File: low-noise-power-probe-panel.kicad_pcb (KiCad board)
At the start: 4 copper layers, 79.8 x 124.8 mm, 118 parts, among them J1 Amphenol 031-5431-10RFX, J10 RF Shield Clip, J11 RF Shield Clip, J12 RF Shield Clip, J2 Amphenol 031-5431-10RFX, J3 Barrel_Jack, J4 USB_C_Receptacle, J5 CONN_041X04_NO_SILK, J6 RF Shield Clip, J7 RF Shield Clip, J8 RF Shield Clip, J9 RF Shield Clip, Q1 WSE3099, SW1 SW_3PDT_x3, U1 OPA322, U2 OPA322, U3 ADP7142AUJZ-2.5, U4 MCP73213T-A6SI/MF, U5 ADP7182AUJZ-2.5, U6 HUSB238, U7 LM334DT, U8 LM311DR

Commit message: add panel and gerbers for v2.0
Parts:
- removed C19: 27pF, Capacitor_SMD:C_0201_0603Metric
- removed C26: DNP, Capacitor_SMD:C_0402_1005Metric
- removed C27, C28: 4.7u, Capacitor_SMD:C_0805_2012Metric
- removed J10, J6, J7: RF Shield Clip, misc:ICSRC6508-015SFR
- removed J5: CONN_041X04_NO_SILK, Connector_PinHeader_2.54mm:PinHeader_1x04_P2.54mm_Vertical
- removed R25: 6.04k, Resistor_SMD:R_0603_1608Metric
- removed TP14: U1_OUT, rf-connectors:U.FL-Hirose
- removed TP16: V_UNREG, rf-connectors:U.FL-Hirose
- removed TP17: +V_BATCHG, rf-connectors:U.FL-Hirose
- removed TP18: +V_BAT, rf-connectors:U.FL-Hirose
- removed TP19: -V_BAT, rf-connectors:U.FL-Hirose
- added C15: 100n, Capacitor_SMD:C_0402_1005Metric, B.Cu at (230.5, 76.1)
- added C16: 100n, Capacitor_SMD:C_0402_1005Metric, B.Cu at (240.3, 75.2)
- added C17: 100n, Capacitor_SMD:C_0402_1005Metric, B.Cu at (237.7, 77.5)
- added C23: 100n, Capacitor_SMD:C_0402_1005Metric, B.Cu at (205.7, 100.4)
- added F3: SMD1206-050C-24V, Fuse:Fuse_1206_3216Metric, B.Cu at (189.2, 106.0)
- added F4: SMD1206-050C-24V, Fuse:Fuse_1206_3216Metric, B.Cu at (208.2, 106.0)
- added JP1: SolderJumper_2_Bridged, Jumper:SolderJumper-2_P1.3mm_Bridged_RoundedPad1.0x1.5mm, B.Cu at (233.5, 81.7)
- added Q2: HL2312, Package_TO_SOT_SMD:SOT-23, B.Cu at (210.4, 99.9)
- added Q3: HL2312, Package_TO_SOT_SMD:SOT-23, B.Cu at (210.4, 96.4)
- added R11: 100R, Resistor_SMD:R_0603_1608Metric, B.Cu at (230.2, 77.4)
- added R27: 160R, Resistor_SMD:R_0603_1608Metric, B.Cu at (239.8, 76.5)
- added R28: 260R, Resistor_SMD:R_0603_1608Metric, B.Cu at (239.8, 78.1)
- added R29: 100R, Resistor_SMD:R_0603_1608Metric, B.Cu at (239.8, 79.7)
- added R30: 50k, Resistor_SMD:R_0603_1608Metric, B.Cu at (230.2, 79.0)
- added R31: 1k, Resistor_SMD:R_0603_1608Metric, B.Cu at (204.7, 97.5)
- added R32: 100R, Resistor_SMD:R_0603_1608Metric, B.Cu at (207.0, 100.9)
- added R33: 100R, Resistor_SMD:R_0603_1608Metric, B.Cu at (204.4, 100.9)
- added REF**: MountingHole_3.2mm_M3, MountingHole:MountingHole_3.2mm_M3, F.Cu at (177.8, 73.5)
- added REF**: MountingHole_3.2mm_M3, MountingHole:MountingHole_3.2mm_M3, F.Cu at (219.8, 73.5)
- added U10: S-82C2AAB-I6T1U7, misc:S-82C2A_Battery_Protection_2S, B.Cu at (206.8, 97.5)
- added U9: ~, Package_SON:VSON-8-1EP_3x3mm_P0.65mm_EP1.65x2.4mm, B.Cu at (235.1, 78.2)
- C1, C22, C25, C3, J11, J12, J8, J9, R1, R2, R26, R3, R4, R5, R6, R7, U1, U2: moved to F.Cu
- C18, C20: value DNP -> 100n
- C29, C30: moved to B.Cu
- F1, F2: value 30V 500mA 150ms -> SMD1206-050C-24V
- J1, J2: value Amphenol 031-5431-10RFX -> Amphenol 132203-12; footprint rf-connectors:BNC_Amphenol_031-5431-10RFX_Horizontal -> Connector_Coaxial:SMA_Amphenol_132203-12_Horizontal
- J3: value Barrel_Jack -> DC-005 2.0
- L1: footprint Inductor_SMD:L_1210_3225Metric -> Inductor_SMD:L_1812_4532Metric; moved to F.Cu
- R15: value 6.04k -> 10M; moved to F.Cu
- R23: value 50k -> 1k
- TP1, TP12, TP2: footprint TestPoint:TestPoint_Keystone_5000-5004_Miniature -> TestPoint:TestPoint_Pad_D2.0mm; moved to F.Cu
- TP3, TP4, TP7, TP8, TP9: footprint TestPoint:TestPoint_Keystone_5000-5004_Miniature -> TestPoint:TestPoint_Pad_D2.0mm
- moved R15 60.6 mm to (199.6, 120.8), turned to 180 degrees
- moved C2 55.2 mm to (236.1, 80.5), turned to 0 degrees
- moved C18 53.1 mm to (232.3, 77.5), turned to -90 degrees
- moved TP8 20.6 mm to (218.2, 114.4)
- moved TP3 18.6 mm to (198.6, 114.4)
- moved C29 17.5 mm to (201.2, 125.2)
- moved TP5 17.5 mm to (204.7, 123.1), turned to 90 degrees
- moved C20 17.2 mm to (203.1, 100.4), turned to 90 degrees
- moved TP10 16.0 mm to (212.1, 123.1), turned to 90 degrees
- moved TP4 15.6 mm to (199.8, 121.4)
- moved TP9 14.2 mm to (217.0, 121.4)
- moved C4 14.0 mm to (207.2, 124.3), turned to -90 degrees
- moved R26 13.2 mm to (200.9, 119.2), turned to 0 degrees
- moved J8 13.0 mm to (190.4, 123.7), turned to 90 degrees
- moved C8 12.5 mm to (205.2, 119.2)
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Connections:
- net Board_0-Net-(BT1A--) renamed Board_0-/MID_BAT_D
- net Board_0-Net-(C26-Pad2) renamed Board_0-Net-(L1-Pad1)
- C18 pad 1: Board_0-Net-(J1-In) -> Board_0-/USB_VGND
- C18 pad 2: Board_0-Net-(C1-Pad2) -> Board_0-/BAL_VDD
- C2 pad 1: Board_0-/PROBE_VGND -> Board_0-/USB_VGND
- C2 pad 2: Board_0-Net-(C2-Pad2) -> Board_0-Net-(U9-CD)
- C20 pad 1: Board_0-Net-(U1--) -> Board_0-/-V_BAT_D
- C20 pad 2: Board_0-Net-(TP14-SIGNAL) -> Board_0-Net-(U10-VC)
- R15 pad 1: Board_0-/SDA -> Board_0-Net-(U1--)
- R15 pad 2: Board_0-Net-(J5-Pin_1) -> Board_0-/PROBE_VGND
- R26 pad 2: Board_0-Net-(TP14-SIGNAL) -> Board_0-Net-(R26-Pad2)
- R3 pad 1: Board_0-Net-(TP14-SIGNAL) -> Board_0-Net-(R26-Pad2)
- R5 pad 2: Board_0-Net-(C2-Pad2) -> Board_0-Net-(R5-Pad2)
- R6 pad 2: Board_0-Net-(TP14-SIGNAL) -> Board_0-Net-(R26-Pad2)
- RV1 pad 2: Board_0-Net-(C2-Pad2) -> Board_0-Net-(R5-Pad2)
- SW1 pad 2: Board_0-Net-(BT1A-+) -> Board_0-/+V_BAT_D
- SW1 pad 5: Board_0-Net-(BT1B--) -> Board_0-/-V_BAT_L
- SW1 pad 7: Board_0-unconnected-(SW1C-A-Pad7) -> Board_0-/MID_BATCHG
- U1 pad 1: Board_0-Net-(TP14-SIGNAL) -> Board_0-Net-(R26-Pad2)
- U6 pad 6: Board_0-/SDA -> Board_0-unconnected-(U6-SDA-Pad6)
- U6 pad 7: Board_0-/SCL -> Board_0-unconnected-(U6-SCL-Pad7)
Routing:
- net Board_0-/+V_BAT_D: track 0.00 -> 59.3 mm, vias 0 -> 2
- net Board_0-Net-(BT1A-+): track 55.2 -> 3.88 mm, vias 2 -> 0
- net Board_0-/SDA: track 50.4 -> 0.00 mm
- net Board_0-/-V_BAT_L: track 0.00 -> 50.3 mm, vias 0 -> 2
- net Board_0-/MID_BATCHG: track 0.00 -> 42.3 mm, vias 0 -> 1
- net Board_0-/SCL: track 40.7 -> 0.00 mm
- net Board_0-/MID_BAT_D: track 128.0 -> 163.9 mm, vias 0 -> 1
- net Board_0-Net-(BT1B--): track 36.8 -> 3.88 mm
- net Board_0--2V5: track 88.1 -> 58.6 mm, vias 4 -> 2
- net Board_0-+2V5: track 81.0 -> 55.9 mm, vias 4 -> 2
- net Board_0-Net-(C2-Pad2): track 22.0 -> 0.00 mm
- net Board_0-Net-(R5-Pad2): track 0.00 -> 18.5 mm, vias 0 -> 1
- net Board_0-/+V_BATCHG: track 50.8 -> 68.9 mm, vias 0 -> 2
- net Board_0-Net-(D3-A): track 51.8 -> 33.9 mm
- net Board_0-/-V_BAT_D: track 0.00 -> 13.3 mm
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- added copper zone on In3.Cu, net Board_0-/PROBE_VGND
- added copper zone on In4.Cu, net Board_0-/PROBE_VGND
- added copper zone on In3.Cu, net Board_0-/USB_VGND
- added copper zone on In4.Cu, net Board_0-/USB_VGND
- added copper zone on In2.Cu, net Board_0-/V_UNREG
- removed copper zone on B.Cu, net Board_0-+2V5
- removed copper zone on B.Cu, net Board_0--2V5
- removed copper zone on B.Cu, net Board_0-/+V_BAT
- removed copper zone on B.Cu, net Board_0-/-V_BAT
- removed copper zone on In1.Cu, net Board_0-/V_UNREG
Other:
- copper layers 4 -> 6
- board text added: "+/- 2.5V REGULATOR"
- board text added: "AMPHENOL 132203-12"
- board text added: "BATTERY BALANCING"
- board text added: "BATTERY CHARGE"
- board text added: "BATTERY PROTECTION"
- board text added: "BOURNS 3590P-2-502L"
- board text added: "ENABLE"
- board text added: "FUSE"
- board text added: "L5"
- board text added: "L6"
- board text added: "MASACH MS350-20S"
- board text added: "MAX OFFSET: ±20V ACTIVE SIGNAL: ±1V INPUT IMPEDANCE: 50kΩ (→ 50Ω SCOPE) ATTENUATION: MAX. 1:1.2 v2.0 2025-07-12"
- board text added: "OPA322 x2"
- board text added: "USB-C PD"
- board text added: "low noise power probe v2.0 JLCJLCJLCJLC"
- board text removed: "AMPHENOL 031-5431-10RFX"
- board text removed: "GND"
- board text removed: "HUSB238"
- board text removed: "MAX OFFSET: ±20V ACTIVE SIGNAL: ±1V INPUT IMPEDANCE: 50kΩ (→ 50Ω SCOPE) ATTENUATION: MAX. 1:1.2 v1.0.1 2024-06-23"
- board text removed: "NIDEC M-1305 5K W/W"
- board text removed: "SCL"
- board text removed: "SDA"
- board text removed: "VCC"
- board text removed: "low noise power probe v1.0.1"

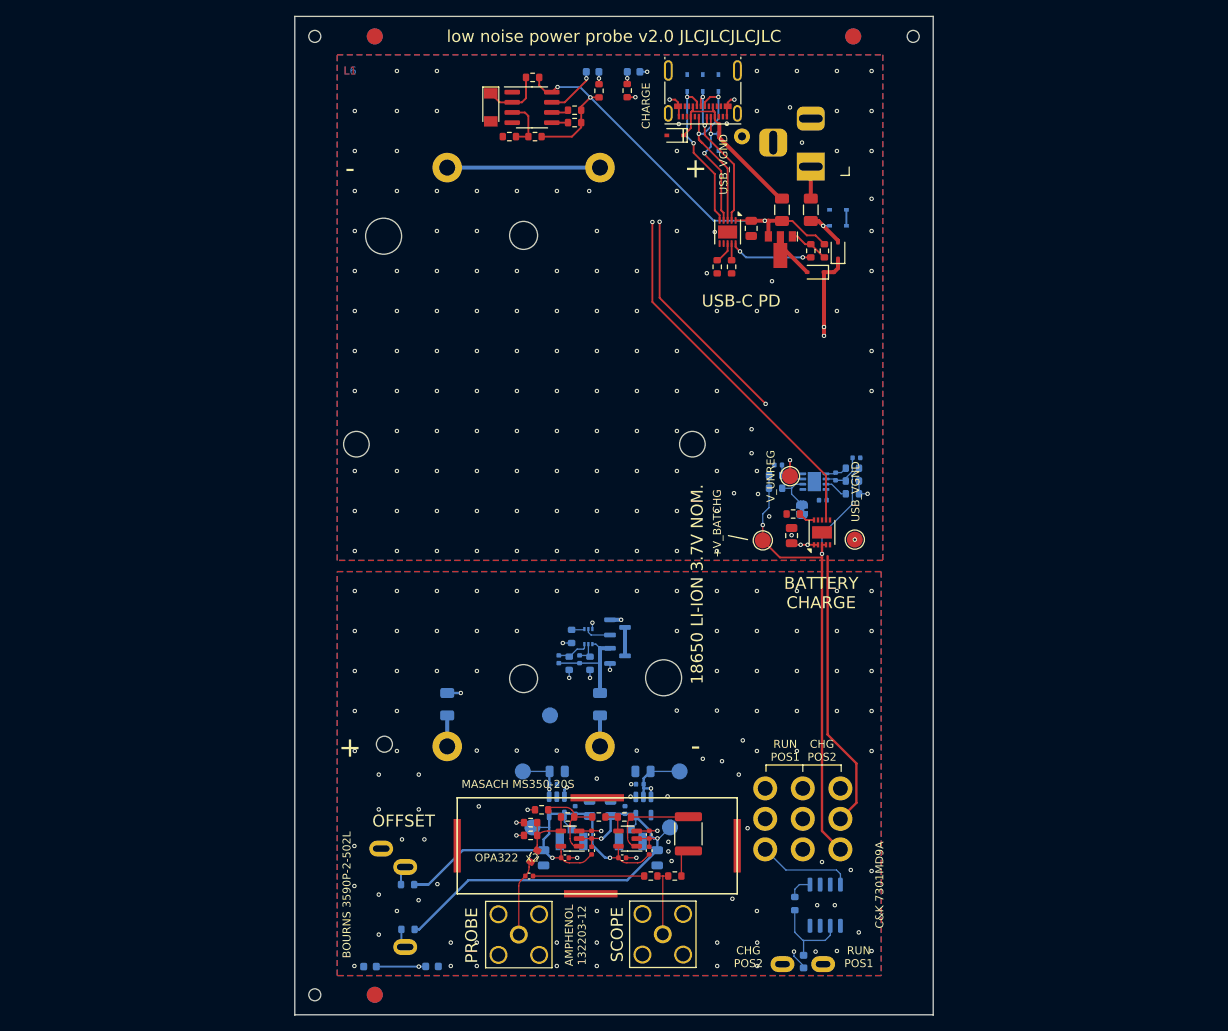
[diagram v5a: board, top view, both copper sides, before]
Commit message: v2.0, as manufactured and tested
Add v2.0. The schematic contains some additional revisions beyond the
BOM to improve frequency response.
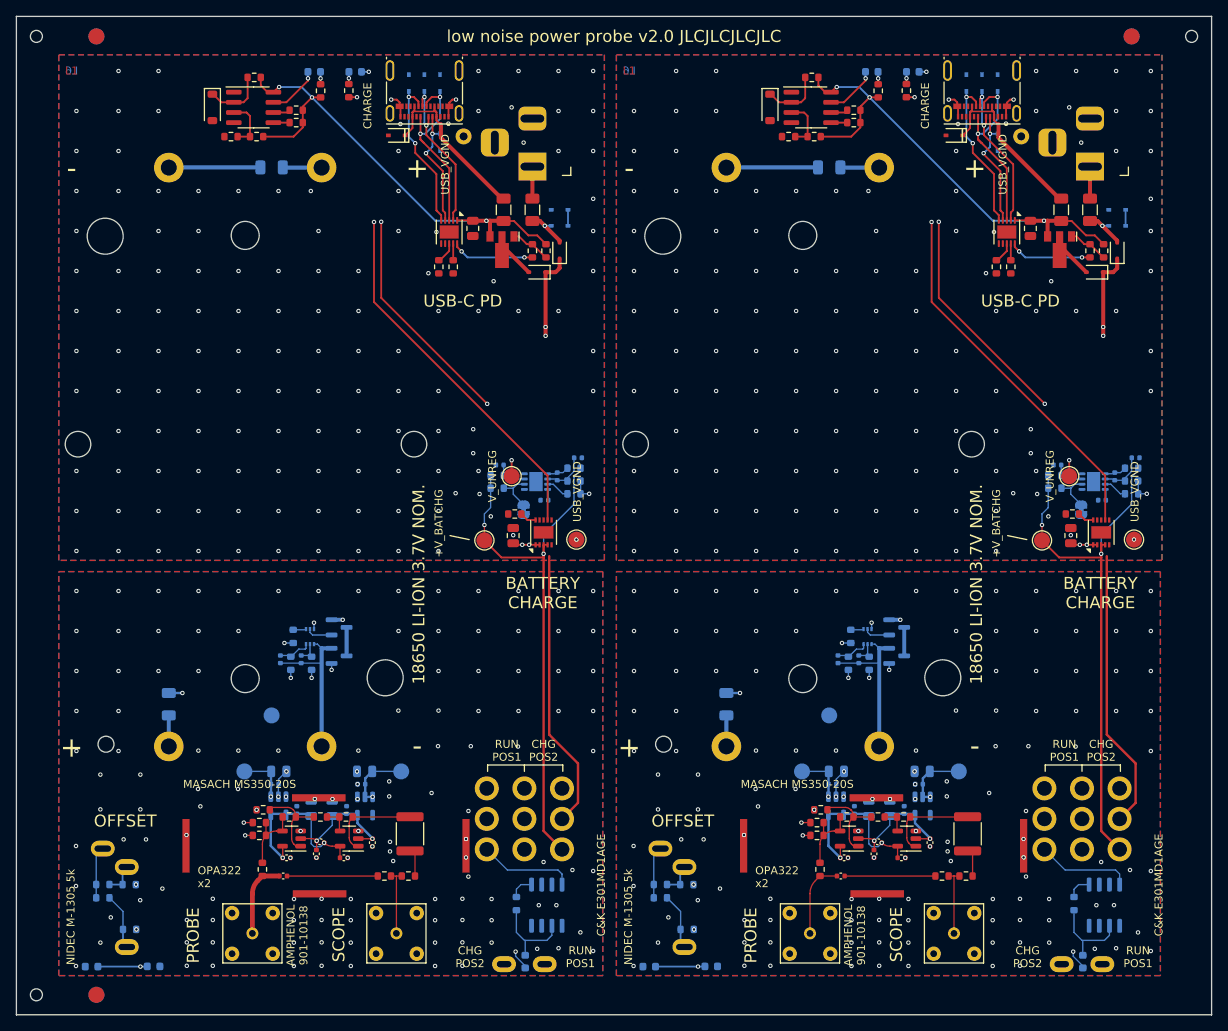
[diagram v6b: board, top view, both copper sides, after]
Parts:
- removed the BT1 at (198.7, 75.1)
- removed the C1 at (199.4, 127.5)
- removed the C10 at (213.6, 114.4)
- removed the C11 at (213.2, 116.0)
- removed the C12 at (209.6, 119.0)
- removed the C13 at (211.4, 119.2)
- removed the C14 at (227.2, 46.5)
- removed the C15 at (230.5, 76.1)
- removed the C16 at (240.3, 75.2)
- removed the C17 at (237.7, 77.5)
- removed the C18 at (232.3, 77.5)
- removed the C2 at (236.1, 80.5)
- removed the C20 at (203.1, 100.4)
- removed the C21 at (203.9, 125.2)
- removed the C22 at (207.2, 122.3)
- removed the C23 at (205.7, 100.4)
- removed the C24 at (211.0, 125.2)
- removed the C25 at (214.4, 122.3)
- removed C29, C30: 4.7u, Capacitor_SMD:C_0805_2012Metric
- removed C3: DNP, Capacitor_SMD:C_0402_1005Metric
- removed the C4 at (207.2, 124.3)
- removed the C5 at (202.9, 114.4)
- removed the C6 at (202.4, 116.0)
- removed the C7 at (206.9, 119.0)
- removed the C8 at (205.2, 119.2)
- removed the C9 at (232.2, 84.9)
- removed the D1 at (207.3, 26.9)
- removed the D10 at (219.2, 28.3)
- removed the D11 at (223.1, 28.3)
- removed the D12 at (221.1, 28.3)
- removed the D13 at (238.0, 44.2)
- removed the D14 at (217.7, 34.9)
- removed the D15 at (238.0, 46.2)
- removed the D2 at (194.6, 31.4)
- removed the D3 at (179.5, 138.8)
- removed the D4 at (187.2, 138.8)
- removed the D5 at (212.4, 26.9)
- removed the D6 at (233.7, 138.2)
- removed the D7 at (238.0, 49.3)
- removed the D8 at (235.2, 52.0)
- removed the D9 at (223.1, 35.7)
- removed the F1 at (234.6, 44.2)
- removed the F2 at (231.0, 44.2)
- removed the F3 at (189.2, 106.0)
- removed the F4 at (208.2, 106.0)
- removed the J1 at (198.1, 134.8)
- removed the J11 at (207.1, 129.7)
- removed the J12 at (225.4, 123.7)
- removed the J2 at (216.1, 134.7)
- removed the J3 at (234.6, 38.8)
- removed the J4 at (221.1, 29.3)
- removed the J8 at (190.4, 123.7)
- removed the J9 at (207.9, 117.7)
- removed the JP1 at (233.5, 81.7)
- removed the L1 at (219.3, 122.2)
- removed the Q1 at (230.8, 49.1)
- removed the Q2 at (210.4, 99.9)
- removed the Q3 at (210.4, 96.4)
- removed the R1 at (214.6, 127.5)
- removed the R10 at (236.3, 49.3)
- removed the R11 at (230.2, 77.4)
- removed the R12 at (234.6, 49.3)
- removed the R13 at (224.7, 51.3)
- removed the R14 at (222.9, 51.3)
- removed the R15 at (199.6, 120.8)
- removed the R16 at (184.2, 134.1)
- removed the R17 at (184.2, 128.5)
- removed the R18 at (205.1, 33.3)
- removed the R19 at (205.1, 31.7)
- removed the R2 at (200.0, 125.0)
- removed the R20 at (232.6, 130.9)
- removed the R21 at (208.1, 29.3)
- removed the R22 at (200.1, 35.0)
- removed the R23 at (199.8, 27.6)
- removed the R24 at (196.9, 35.0)
- removed the R26 at (200.9, 119.2)
- removed the R27 at (239.8, 76.5)
- removed the R28 at (239.8, 78.1)
- removed the R29 at (239.8, 79.7)
- removed the R3 at (204.2, 120.1)
- removed the R30 at (230.2, 79.0)
- removed the R31 at (204.7, 97.5)
- removed the R32 at (207.0, 100.9)
- removed the R33 at (204.4, 100.9)
- removed the R4 at (211.3, 120.1)
- removed the R5 at (199.6, 122.4)
- removed the R6 at (208.1, 120.1)
- removed the R7 at (217.6, 127.5)
- removed the R8 at (211.7, 29.3)
- removed the R9 at (232.4, 82.2)
- removed REF** (x2): MountingHole_3.2mm_M3, MountingHole:MountingHole_3.2mm_M3
- removed the RV1 at (183.9, 136.3)
- removed the SW1 at (234.8, 127.9)
- removed the TP1 at (232.0, 77.5)
- removed TP10: -2V5, rf-connectors:U.FL-Hirose
- removed the TP12 at (240.1, 85.4)
- removed the TP2 at (228.6, 85.5)
- removed the TP21 at (226.0, 35.0)
- removed the TP3 at (198.6, 114.4)
- removed TP4: +2V5, TestPoint:TestPoint_Pad_D2.0mm
- removed TP5: +2V5, rf-connectors:U.FL-Hirose
- removed the TP7 at (202.0, 107.4)
- removed the TP8 at (218.2, 114.4)
- removed TP9: -2V5, TestPoint:TestPoint_Pad_D2.0mm
- removed the U1 at (204.5, 122.8)
- removed the U10 at (206.8, 97.5)
- removed the U2 at (211.7, 122.8)
- removed the U3 at (202.8, 118.7)
- removed the U4 at (236.0, 84.5)
- removed the U5 at (213.7, 118.7)
- removed the U6 at (224.2, 47.0)
- removed the U7 at (236.4, 131.1)
- removed the U8 at (199.8, 31.4)
- removed the U9 at (235.1, 78.2)
- added BT1: Dual_Battery_Cell, misc:Battery-holder-18650-MYOUNG-BH-18650-A1BJ021, F.Cu at (163.9, 75.1)
- added BT1: Dual_Battery_Cell, misc:Battery-holder-18650-MYOUNG-BH-18650-A1BJ021, F.Cu at (233.6, 75.1)
- added C1: 100n / SRF 28MHz, Capacitor_SMD:C_0402_1005Metric, F.Cu at (238.3, 127.5)
- added C1: 100n / SRF 28MHz, Capacitor_SMD:C_0402_1005Metric, F.Cu at (168.7, 127.5)
- added C10: 4.7u, Capacitor_SMD:C_0805_2012Metric, B.Cu at (248.5, 114.4)
- added C10: 4.7u, Capacitor_SMD:C_0805_2012Metric, B.Cu at (178.8, 114.4)
- added C11: 2.2u, Capacitor_SMD:C_0402_1005Metric, B.Cu at (248.1, 116.0)
- added C11: 2.2u, Capacitor_SMD:C_0402_1005Metric, B.Cu at (178.4, 116.0)
- added C12: 4.7u, Capacitor_SMD:C_0805_2012Metric, B.Cu at (174.8, 119.0)
- added C12: 4.7u, Capacitor_SMD:C_0805_2012Metric, B.Cu at (244.5, 119.0)
- added C13: 2.2u, Capacitor_SMD:C_0402_1005Metric, B.Cu at (176.6, 119.2)
- added C13: 2.2u, Capacitor_SMD:C_0402_1005Metric, B.Cu at (246.3, 119.2)
- added C14: 4.7u, Capacitor_SMD:C_0805_2012Metric, F.Cu at (192.3, 46.5)
- added C14: 4.7u, Capacitor_SMD:C_0805_2012Metric, F.Cu at (262.1, 46.5)
- added C15: 100n, Capacitor_SMD:C_0402_1005Metric, B.Cu at (265.4, 76.1)
- added C15: 100n, Capacitor_SMD:C_0402_1005Metric, B.Cu at (195.7, 76.1)
- added C16: 100n, Capacitor_SMD:C_0402_1005Metric, B.Cu at (275.2, 75.2)
- added C16: 100n, Capacitor_SMD:C_0402_1005Metric, B.Cu at (205.5, 75.2)
- added C17: 100n, Capacitor_SMD:C_0402_1005Metric, B.Cu at (202.9, 77.5)
- added C17: 100n, Capacitor_SMD:C_0402_1005Metric, B.Cu at (272.6, 77.5)
- added C18: 100n, Capacitor_SMD:C_0402_1005Metric, B.Cu at (197.5, 77.5)
- added C18: 100n, Capacitor_SMD:C_0402_1005Metric, B.Cu at (267.2, 77.5)
- added C2: 100n, Capacitor_SMD:C_0402_1005Metric, B.Cu at (201.3, 80.5)
- added C2: 100n, Capacitor_SMD:C_0402_1005Metric, B.Cu at (271.0, 80.5)
- added C20: 100n, Capacitor_SMD:C_0402_1005Metric, B.Cu at (168.3, 100.4)
- added C20: 100n, Capacitor_SMD:C_0402_1005Metric, B.Cu at (238.0, 100.4)
- added C21: 2.2u, Capacitor_SMD:C_0402_1005Metric, F.Cu at (169.1, 125.2)
- added C21: 2.2u, Capacitor_SMD:C_0402_1005Metric, F.Cu at (238.8, 125.2)
- added C22: 2.2u, Capacitor_SMD:C_0402_1005Metric, F.Cu at (172.8, 124.7)
- added C22: 2.2u, Capacitor_SMD:C_0402_1005Metric, F.Cu at (242.5, 124.7)
- added C23: 100n, Capacitor_SMD:C_0402_1005Metric, B.Cu at (170.9, 100.4)
- added C23: 100n, Capacitor_SMD:C_0402_1005Metric, B.Cu at (240.6, 100.4)
- added C24: 2.2u, Capacitor_SMD:C_0402_1005Metric, F.Cu at (245.9, 125.2)
- added C24: 2.2u, Capacitor_SMD:C_0402_1005Metric, F.Cu at (176.2, 125.2)
- added C25: 2.2u, Capacitor_SMD:C_0402_1005Metric, F.Cu at (179.8, 123.3)
- added C25: 2.2u, Capacitor_SMD:C_0402_1005Metric, F.Cu at (249.5, 123.3)
- added C4: 2.2u, Capacitor_SMD:C_0402_1005Metric, F.Cu at (243.0, 123.2)
- added C4: 2.2u, Capacitor_SMD:C_0402_1005Metric, F.Cu at (173.3, 123.2)
- added C5: 4.7u, Capacitor_SMD:C_0805_2012Metric, B.Cu at (168.1, 114.4)
- added C5: 4.7u, Capacitor_SMD:C_0805_2012Metric, B.Cu at (237.8, 114.4)
- added C6: 2.2u, Capacitor_SMD:C_0402_1005Metric, B.Cu at (167.6, 116.0)
- added C6: 2.2u, Capacitor_SMD:C_0402_1005Metric, B.Cu at (237.3, 116.0)
- added C7: 4.7u, Capacitor_SMD:C_0805_2012Metric, B.Cu at (241.8, 119.0)
- added C7: 4.7u, Capacitor_SMD:C_0805_2012Metric, B.Cu at (172.2, 119.0)
- added C8: 2.2u, Capacitor_SMD:C_0402_1005Metric, B.Cu at (170.3, 119.2)
- added C8: 2.2u, Capacitor_SMD:C_0402_1005Metric, B.Cu at (240.1, 119.2)
- added C9: 4.7u, Capacitor_SMD:C_0805_2012Metric, F.Cu at (267.1, 84.9)
- added C9: 4.7u, Capacitor_SMD:C_0805_2012Metric, F.Cu at (197.4, 84.9)
- added D1: Red 1.8V, misc:LED_0603_1608Metric_polaritysilk, B.Cu at (242.2, 26.9)
- added D1: Red 1.8V, misc:LED_0603_1608Metric_polaritysilk, B.Cu at (172.5, 26.9)
- added D10: SD24-MS, misc:D_SOD-323_silkpolarity, B.Cu at (254.1, 28.3)
- added D10: SD24-MS, misc:D_SOD-323_silkpolarity, B.Cu at (184.3, 28.3)
- added D11: SD24-MS, misc:D_SOD-323_silkpolarity, B.Cu at (188.2, 28.3)
- added D11: SD24-MS, misc:D_SOD-323_silkpolarity, B.Cu at (257.9, 28.3)
- added D12: SD24-MS, misc:D_SOD-323_silkpolarity, B.Cu at (186.3, 28.3)
- added D12: SD24-MS, misc:D_SOD-323_silkpolarity, B.Cu at (256.0, 28.3)
- added D13: SD24-MS, misc:D_SOD-323_silkpolarity, B.Cu at (272.9, 44.2)
- added D13: SD24-MS, misc:D_SOD-323_silkpolarity, B.Cu at (203.2, 44.2)
- added D14: SD24-MS, misc:D_SOD-323_silkpolarity, F.Cu at (252.6, 34.9)
- added D14: SD24-MS, misc:D_SOD-323_silkpolarity, F.Cu at (182.8, 34.9)
- added D15: SD24-MS, misc:D_SOD-323_silkpolarity, B.Cu at (203.2, 46.2)
- added D15: SD24-MS, misc:D_SOD-323_silkpolarity, B.Cu at (272.9, 46.2)
- added D2: 3V3, Diode_SMD:D_SOD-123, F.Cu at (229.5, 31.4)
- added D2: 3V3, Diode_SMD:D_SOD-123, F.Cu at (159.8, 31.4)
- added D3: Red 1.8V, misc:LED_0603_1608Metric_polaritysilk, B.Cu at (144.7, 138.8)
- added D3: Red 1.8V, misc:LED_0603_1608Metric_polaritysilk, B.Cu at (214.4, 138.8)
- added D4: Red 1.8V, misc:LED_0603_1608Metric_polaritysilk, B.Cu at (152.4, 138.8)
- added D4: Red 1.8V, misc:LED_0603_1608Metric_polaritysilk, B.Cu at (222.2, 138.8)
- added D5: Red 1.8V, misc:LED_0603_1608Metric_polaritysilk, B.Cu at (247.3, 26.9)
- added D5: Red 1.8V, misc:LED_0603_1608Metric_polaritysilk, B.Cu at (177.7, 26.9)
- added D6: Red 1.8V, misc:LED_0603_1608Metric_polaritysilk, B.Cu at (268.6, 138.2)
- added D6: Red 1.8V, misc:LED_0603_1608Metric_polaritysilk, B.Cu at (198.9, 138.2)
- added D7: 1N5819WS, Diode_SMD:D_SOD-323, F.Cu at (203.2, 49.3)
- added D7: 1N5819WS, Diode_SMD:D_SOD-323, F.Cu at (272.9, 49.3)
- added D8: 1N5819WS, Diode_SMD:D_SOD-323, F.Cu at (200.4, 52.0)
- added D8: 1N5819WS, Diode_SMD:D_SOD-323, F.Cu at (270.1, 52.0)
- added D9: SD24-MS, misc:D_SOD-323_silkpolarity, B.Cu at (257.9, 35.7)
- added D9: SD24-MS, misc:D_SOD-323_silkpolarity, B.Cu at (188.2, 35.7)
- added F1: SMD1206-050C-24V, Fuse:Fuse_1206_3216Metric, F.Cu at (199.8, 44.2)
- added F1: SMD1206-050C-24V, Fuse:Fuse_1206_3216Metric, F.Cu at (269.5, 44.2)
- added F2: SMD1206-050C-24V, Fuse:Fuse_1206_3216Metric, F.Cu at (196.2, 44.2)
- added F2: SMD1206-050C-24V, Fuse:Fuse_1206_3216Metric, F.Cu at (265.9, 44.2)
- added F3: SMD1206-050C-24V, Fuse:Fuse_1206_3216Metric, B.Cu at (224.1, 106.0)
- added F3: SMD1206-050C-24V, Fuse:Fuse_1206_3216Metric, B.Cu at (154.3, 106.0)
- added F4: SMD1206-050C-24V, Fuse:Fuse_1206_3216Metric, B.Cu at (167.2, 38.9)
- added F4: SMD1206-050C-24V, Fuse:Fuse_1206_3216Metric, B.Cu at (236.9, 38.9)
- added J1: Amphenol 901-10138, rf-connectors:SMA_Amphenol_901-10138_Horizontal, F.Cu at (234.5, 134.6)
- added J1: Amphenol 901-10138, rf-connectors:SMA_Amphenol_901-10138_Horizontal, F.Cu at (164.8, 134.6)
- added J11: RF Shield Clip, misc:ICSRC6508-015SFR, F.Cu at (173.2, 129.7)
- added J11: RF Shield Clip, misc:ICSRC6508-015SFR, F.Cu at (242.9, 129.7)
- added J12: RF Shield Clip, misc:ICSRC6508-015SFR, F.Cu at (191.5, 123.7)
- added J12: RF Shield Clip, misc:ICSRC6508-015SFR, F.Cu at (261.2, 123.7)
- added J2: Amphenol 901-10138, rf-connectors:SMA_Amphenol_901-10138_Horizontal, F.Cu at (182.8, 134.6)
- added J2: Amphenol 901-10138, rf-connectors:SMA_Amphenol_901-10138_Horizontal, F.Cu at (252.5, 134.6)
- added J3: DC-005 2.0, Connector_BarrelJack:BarrelJack_Horizontal, F.Cu at (269.5, 38.8)
- added J3: DC-005 2.0, Connector_BarrelJack:BarrelJack_Horizontal, F.Cu at (199.8, 38.8)
- added J4: USB_C_Receptacle, Connector_USB:USB_C_Receptacle_Molex_105450-0101, F.Cu at (186.3, 29.3)
- added J4: USB_C_Receptacle, Connector_USB:USB_C_Receptacle_Molex_105450-0101, F.Cu at (256.0, 29.3)
- added J8: RF Shield Clip, misc:ICSRC6508-015SFR, F.Cu at (226.2, 123.7)
- added J8: RF Shield Clip, misc:ICSRC6508-015SFR, F.Cu at (156.5, 123.7)
- added J9: RF Shield Clip, misc:ICSRC6508-015SFR, F.Cu at (242.8, 117.7)
- added J9: RF Shield Clip, misc:ICSRC6508-015SFR, F.Cu at (173.1, 117.7)
- added JP1: SolderJumper_2_Bridged, Jumper:SolderJumper-2_P1.3mm_Bridged_RoundedPad1.0x1.5mm, B.Cu at (268.4, 81.7)
- added JP1: SolderJumper_2_Bridged, Jumper:SolderJumper-2_P1.3mm_Bridged_RoundedPad1.0x1.5mm, B.Cu at (198.7, 81.7)
- added L1: 10uH 5%, Inductor_SMD:L_1812_4532Metric, F.Cu at (254.2, 122.2)
- added L1: 10uH 5%, Inductor_SMD:L_1812_4532Metric, F.Cu at (184.5, 122.2)
- added NPTH1: MountingHole_3.2mm_M3, MountingHole:MountingHole_3.2mm_M3, F.Cu at (212.7, 73.5)
- added NPTH1: MountingHole_3.2mm_M3, MountingHole:MountingHole_3.2mm_M3, F.Cu at (143.0, 73.5)
- added NPTH2: MountingHole_3.2mm_M3, MountingHole:MountingHole_3.2mm_M3, F.Cu at (254.7, 73.5)
- added NPTH2: MountingHole_3.2mm_M3, MountingHole:MountingHole_3.2mm_M3, F.Cu at (185.0, 73.5)
- added Q1: WSE3099, Package_TO_SOT_SMD:SOT-89-3, F.Cu at (196.0, 49.1)
- added Q1: WSE3099, Package_TO_SOT_SMD:SOT-89-3, F.Cu at (265.7, 49.1)
- added Q2: HL2312, Package_TO_SOT_SMD:SOT-23, B.Cu at (245.3, 99.9)
- added Q2: HL2312, Package_TO_SOT_SMD:SOT-23, B.Cu at (175.6, 99.9)
- added Q3: HL2312, Package_TO_SOT_SMD:SOT-23, B.Cu at (245.3, 96.4)
- added Q3: HL2312, Package_TO_SOT_SMD:SOT-23, B.Cu at (175.6, 96.4)
- added R1: 10R 1% 200ppm/°C, Resistor_SMD:R_0603_1608Metric, F.Cu at (181.3, 127.5)
- added R1: 10R 1% 200ppm/°C, Resistor_SMD:R_0603_1608Metric, F.Cu at (251.0, 127.5)
- added R10: 50k, Resistor_SMD:R_0603_1608Metric, F.Cu at (201.5, 49.3)
- added R10: 50k, Resistor_SMD:R_0603_1608Metric, F.Cu at (271.2, 49.3)
- added R11: 100R, Resistor_SMD:R_0603_1608Metric, B.Cu at (265.1, 77.4)
- added R11: 100R, Resistor_SMD:R_0603_1608Metric, B.Cu at (195.4, 77.4)
- added R12: 6.04k, Resistor_SMD:R_0603_1608Metric, F.Cu at (269.5, 49.3)
- added R12: 6.04k, Resistor_SMD:R_0603_1608Metric, F.Cu at (199.8, 49.3)
- added R13: 0R, Resistor_SMD:R_0603_1608Metric, F.Cu at (259.6, 51.3)
- added R13: 0R, Resistor_SMD:R_0603_1608Metric, F.Cu at (189.9, 51.3)
- added R14: 6.04k, Resistor_SMD:R_0603_1608Metric, F.Cu at (257.8, 51.3)
- added R14: 6.04k, Resistor_SMD:R_0603_1608Metric, F.Cu at (188.1, 51.3)
- added R15: 10M, Resistor_SMD:R_0603_1608Metric, F.Cu at (165.7, 120.8)
- added R15: 10M, Resistor_SMD:R_0603_1608Metric, F.Cu at (235.4, 120.8)
- added R16: 620, Resistor_SMD:R_0603_1608Metric, B.Cu at (219.2, 134.1)
- added R16: 620, Resistor_SMD:R_0603_1608Metric, B.Cu at (149.4, 134.1)
- added R17: 620, Resistor_SMD:R_0603_1608Metric, B.Cu at (219.1, 128.5)
- added R17: 620, Resistor_SMD:R_0603_1608Metric, B.Cu at (149.4, 128.5)
- added R18: DNP, Resistor_SMD:R_0603_1608Metric, F.Cu at (240.0, 33.3)
- added R18: DNP, Resistor_SMD:R_0603_1608Metric, F.Cu at (170.3, 33.3)
- added R19: DNP, Resistor_SMD:R_0603_1608Metric, F.Cu at (170.3, 31.7)
- added R19: DNP, Resistor_SMD:R_0603_1608Metric, F.Cu at (240.0, 31.7)
- added R2: 50k .1%, Resistor_SMD:R_0603_1608Metric, F.Cu at (166.1, 126.6)
- added R2: 50k .1%, Resistor_SMD:R_0603_1608Metric, F.Cu at (235.8, 126.6)
- added R20: 33R, Resistor_SMD:R_0603_1608Metric, B.Cu at (267.5, 130.9)
- added R20: 33R, Resistor_SMD:R_0603_1608Metric, B.Cu at (197.8, 130.9)
- added R21: 1k, Resistor_SMD:R_0603_1608Metric, F.Cu at (173.3, 29.3)
- added R21: 1k, Resistor_SMD:R_0603_1608Metric, F.Cu at (243.0, 29.3)
- added R22: 50k, Resistor_SMD:R_0603_1608Metric, F.Cu at (235.0, 35.0)
- added R22: 50k, Resistor_SMD:R_0603_1608Metric, F.Cu at (165.3, 35.0)
- added R23: 1k, Resistor_SMD:R_0603_1608Metric, F.Cu at (234.7, 27.6)
- added R23: 1k, Resistor_SMD:R_0603_1608Metric, F.Cu at (165.0, 27.6)
- added R24: 50k, Resistor_SMD:R_0603_1608Metric, F.Cu at (231.8, 35.0)
- added R24: 50k, Resistor_SMD:R_0603_1608Metric, F.Cu at (162.1, 35.0)
- added R25: 1k .1%, Resistor_SMD:R_0603_1608Metric, B.Cu at (146.1, 130.2)
- added R25: 1k .1%, Resistor_SMD:R_0603_1608Metric, B.Cu at (215.8, 130.2)
- added R26: 0R, Resistor_SMD:R_0603_1608Metric, F.Cu at (166.2, 119.2)
- added R26: 0R, Resistor_SMD:R_0603_1608Metric, F.Cu at (235.8, 119.2)
- added R27: 150R, Resistor_SMD:R_0603_1608Metric, B.Cu at (205.0, 76.5)
- added R27: 150R, Resistor_SMD:R_0603_1608Metric, B.Cu at (274.7, 76.5)
- added R28: 270R, Resistor_SMD:R_0603_1608Metric, B.Cu at (274.7, 78.1)
- added R28: 270R, Resistor_SMD:R_0603_1608Metric, B.Cu at (205.0, 78.1)
- added R29: 100R, Resistor_SMD:R_0603_1608Metric, B.Cu at (274.7, 79.7)
- added R29: 100R, Resistor_SMD:R_0603_1608Metric, B.Cu at (205.0, 79.7)
- added R3: 50k .1%, Resistor_SMD:R_0603_1608Metric, F.Cu at (239.1, 120.1)
- added R3: 50k .1%, Resistor_SMD:R_0603_1608Metric, F.Cu at (169.4, 120.1)
- added R30: 50k, Resistor_SMD:R_0603_1608Metric, B.Cu at (265.1, 79.0)
- added R30: 50k, Resistor_SMD:R_0603_1608Metric, B.Cu at (195.4, 79.0)
- added R31: 1k, Resistor_SMD:R_0603_1608Metric, B.Cu at (169.9, 97.5)
- added R31: 1k, Resistor_SMD:R_0603_1608Metric, B.Cu at (239.6, 97.5)
- added R32: 100R, Resistor_SMD:R_0603_1608Metric, B.Cu at (172.2, 100.9)
- added R32: 100R, Resistor_SMD:R_0603_1608Metric, B.Cu at (241.9, 100.9)
- added R33: 100R, Resistor_SMD:R_0603_1608Metric, B.Cu at (169.6, 100.9)
- added R33: 100R, Resistor_SMD:R_0603_1608Metric, B.Cu at (239.3, 100.9)
- added R34: 1k .1%, Resistor_SMD:R_0603_1608Metric, B.Cu at (215.8, 128.5)
- added R34: 1k .1%, Resistor_SMD:R_0603_1608Metric, B.Cu at (146.1, 128.5)
- added R4: 1k .1%, Resistor_SMD:R_0603_1608Metric, F.Cu at (246.2, 120.1)
- added R4: 1k .1%, Resistor_SMD:R_0603_1608Metric, F.Cu at (176.5, 120.1)
- added R5: 3.3k, Resistor_SMD:R_0603_1608Metric, F.Cu at (165.7, 122.4)
- added R5: 3.3k, Resistor_SMD:R_0603_1608Metric, F.Cu at (235.4, 122.4)
- added R6: 1k .1%, Resistor_SMD:R_0603_1608Metric, F.Cu at (243.0, 120.1)
- added R6: 1k .1%, Resistor_SMD:R_0603_1608Metric, F.Cu at (173.3, 120.1)
- added R7: 10R 1% 200ppm/°C, Resistor_SMD:R_0603_1608Metric, F.Cu at (184.3, 127.5)
- added R7: 10R 1% 200ppm/°C, Resistor_SMD:R_0603_1608Metric, F.Cu at (254.0, 127.5)
- added R8: 1k, Resistor_SMD:R_0603_1608Metric, F.Cu at (246.6, 29.3)
- added R8: 1k, Resistor_SMD:R_0603_1608Metric, F.Cu at (176.8, 29.3)
- added R9: 5k, Resistor_SMD:R_0603_1608Metric, F.Cu at (197.6, 82.2)
- added R9: 5k, Resistor_SMD:R_0603_1608Metric, F.Cu at (267.3, 82.2)
- added RV1: 5k, misc:Potentiometer_Nidec_M-1303, F.Cu at (218.8, 136.3)
- added RV1: 5k, misc:Potentiometer_Nidec_M-1303, F.Cu at (149.1, 136.3)
- added SW1: SW_3PDT_x3, misc:Switch_3PDT_C&K_7301MD9ABE, F.Cu at (269.7, 127.9)
- added SW1: SW_3PDT_x3, misc:Switch_3PDT_C&K_7301MD9ABE, F.Cu at (200.0, 127.9)
- added TP1: V_UNREG, TestPoint:TestPoint_Pad_D2.0mm, F.Cu at (197.2, 77.5)
- added TP1: V_UNREG, TestPoint:TestPoint_Pad_D2.0mm, F.Cu at (266.9, 77.5)
- added TP12: USB_VGND, TestPoint:TestPoint_Pad_D2.0mm, F.Cu at (205.3, 85.4)
- added TP12: USB_VGND, TestPoint:TestPoint_Pad_D2.0mm, F.Cu at (275.0, 85.4)
- added TP2: +V_BATCHG, TestPoint:TestPoint_Pad_D2.0mm, F.Cu at (263.5, 85.5)
- added TP2: +V_BATCHG, TestPoint:TestPoint_Pad_D2.0mm, F.Cu at (193.8, 85.5)
- added TP21: USB_VGND, TestPoint:TestPoint_Keystone_5000-5004_Miniature, B.Cu at (191.2, 35.0)
- added TP21: USB_VGND, TestPoint:TestPoint_Keystone_5000-5004_Miniature, B.Cu at (260.9, 35.0)
- added TP3: +V_BAT, TestPoint:TestPoint_Pad_D2.0mm, B.Cu at (163.8, 114.4)
- added TP3: +V_BAT, TestPoint:TestPoint_Pad_D2.0mm, B.Cu at (233.5, 114.4)
- added TP7: PROBE_VGND, TestPoint:TestPoint_Pad_D2.0mm, B.Cu at (236.9, 107.4)
- added TP7: PROBE_VGND, TestPoint:TestPoint_Pad_D2.0mm, B.Cu at (167.2, 107.4)
- added TP8: -V_BAT, TestPoint:TestPoint_Pad_D2.0mm, B.Cu at (183.4, 114.4)
- added TP8: -V_BAT, TestPoint:TestPoint_Pad_D2.0mm, B.Cu at (253.1, 114.4)
- added U1: OPA322, Package_TO_SOT_SMD:SOT-23-5, F.Cu at (239.4, 122.8)
- added U1: OPA322, Package_TO_SOT_SMD:SOT-23-5, F.Cu at (169.7, 122.8)
- added U10: S-82C2AAB-I6T1U7, misc:S-82C2A_Battery_Protection_2S, B.Cu at (172.0, 97.5)
- added U10: S-82C2AAB-I6T1U7, misc:S-82C2A_Battery_Protection_2S, B.Cu at (241.7, 97.5)
- added U2: OPA322, Package_TO_SOT_SMD:SOT-23-5, F.Cu at (176.9, 122.8)
- added U2: OPA322, Package_TO_SOT_SMD:SOT-23-5, F.Cu at (246.6, 122.8)
- added U3: ADP7142AUJZ-2.5, Package_TO_SOT_SMD:TSOT-23-5, B.Cu at (237.8, 118.7)
- added U3: ADP7142AUJZ-2.5, Package_TO_SOT_SMD:TSOT-23-5, B.Cu at (168.1, 118.7)
- added U4: MCP73213T-A6SI/MF, Package_DFN_QFN:DFN-10-1EP_3x3mm_P0.5mm_EP1.55x2.48mm, F.Cu at (201.2, 84.5)
- added U4: MCP73213T-A6SI/MF, Package_DFN_QFN:DFN-10-1EP_3x3mm_P0.5mm_EP1.55x2.48mm, F.Cu at (270.9, 84.5)
- added U5: ADP7182AUJZ-2.5, Package_TO_SOT_SMD:TSOT-23-5, B.Cu at (178.9, 118.7)
- added U5: ADP7182AUJZ-2.5, Package_TO_SOT_SMD:TSOT-23-5, B.Cu at (248.6, 118.7)
- added U6: HUSB238, Package_DFN_QFN:DFN-10-1EP_3x3mm_P0.5mm_EP1.65x2.38mm, F.Cu at (259.1, 47.0)
- added U6: HUSB238, Package_DFN_QFN:DFN-10-1EP_3x3mm_P0.5mm_EP1.65x2.38mm, F.Cu at (189.4, 47.0)
- added U7: LM334DT, Package_SO:SO-8_3.9x4.9mm_P1.27mm, B.Cu at (271.3, 131.1)
- added U7: LM334DT, Package_SO:SO-8_3.9x4.9mm_P1.27mm, B.Cu at (201.6, 131.1)
- added U8: LM311DR, Package_SO:SOIC-8_3.9x4.9mm_P1.27mm, F.Cu at (164.9, 31.4)
- added U8: LM311DR, Package_SO:SOIC-8_3.9x4.9mm_P1.27mm, F.Cu at (234.7, 31.4)
- added U9: ~, Package_SON:VSON-8-1EP_3x3mm_P0.65mm_EP1.65x2.4mm, B.Cu at (200.2, 78.2)
- added U9: ~, Package_SON:VSON-8-1EP_3x3mm_P0.65mm_EP1.65x2.4mm, B.Cu at (269.9, 78.2)
- moved KiKit_FID_B_1 34.8 mm to (145.3, 22.5)
- moved KiKit_FID_B_2 34.8 mm to (274.7, 22.5)
- moved KiKit_FID_B_3 34.8 mm to (145.3, 142.3)
- moved KiKit_FID_T_1 34.8 mm to (145.3, 22.5)
- moved KiKit_FID_T_2 34.8 mm to (274.7, 22.5)
- moved KiKit_FID_T_3 34.8 mm to (145.3, 142.3)
- moved KiKit_TO_1 34.8 mm to (137.8, 22.5)
- moved KiKit_TO_2 34.8 mm to (282.2, 22.5)
- moved KiKit_TO_3 34.8 mm to (137.8, 142.3)
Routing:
- net Board_1-/MID_BAT_D: track 0.00 -> 171.7 mm, vias 0 -> 1
- net Board_1-/+V_BATCHG: track 0.00 -> 68.5 mm, vias 0 -> 2
- net Board_1-/V_UNREG: track 0.00 -> 64.7 mm, vias 0 -> 8
- net Board_1-/CHARGE_STAT: track 0.00 -> 63.7 mm, vias 0 -> 2
- net Board_1-/USB_VBUS: track 0.00 -> 60.8 mm, vias 0 -> 3
- net Board_1-/+V_BAT_D: track 0.00 -> 59.3 mm, vias 0 -> 2
- net Board_1-/-V_BAT_L: track 0.00 -> 50.0 mm, vias 0 -> 2
- net Board_1--2V5: track 0.00 -> 49.7 mm, vias 0 -> 3
- net Board_1-/+V_BAT: track 0.00 -> 49.3 mm, vias 0 -> 2
- net Board_1-/MID_BATCHG: track 0.00 -> 42.3 mm, vias 0 -> 1
- net Board_1-+2V5: track 0.00 -> 42.0 mm, vias 0 -> 3
- net Board_1-/USB_VGND: track 0.00 -> 40.7 mm, vias 0 -> 130
- net Board_1-Net-(D3-A): track 0.00 -> 33.3 mm, vias 0 -> 2
- net Board_1-Net-(R25-Pad1): track 0.00 -> 24.8 mm, vias 0 -> 1
- net Board_0-Net-(R25-Pad1): track 0.00 -> 24.8 mm, vias 0 -> 1
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- added copper zone on B.Cu, net Board_1-/PROBE_VGND
- added copper zone on F.Cu, net Board_1-/PROBE_VGND
- added copper zone on In1.Cu, net Board_1-/PROBE_VGND
- added copper zone on In2.Cu, net Board_1-/PROBE_VGND
- added copper zone on In3.Cu, net Board_1-/PROBE_VGND
- added copper zone on In4.Cu, net Board_1-/PROBE_VGND
- added copper zone on B.Cu, net Board_1-/USB_VGND
- added copper zone on F.Cu, net Board_1-/USB_VGND
- added copper zone on In1.Cu, net Board_1-/USB_VGND
- added copper zone on In2.Cu, net Board_1-/USB_VGND
- added copper zone on In3.Cu, net Board_1-/USB_VGND
- added copper zone on In4.Cu, net Board_1-/USB_VGND
- added copper zone on In2.Cu, net Board_1-/V_UNREG
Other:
- board size 79.8 x 124.8 mm -> 149.4 x 124.8 mm
- board text added: "AMPHENOL 901-10138"
- board text added: "C&K E301MD1AGE"
- board text added: "NIDEC M-1305 5k"
- board text added: "Stackup: JLC06161H-3313 impedance controlled 1.6mm total thickness ENIG finish Blue soldermask"
- board text removed: "AMPHENOL 132203-12"
- board text removed: "BOURNS 3590P-2-502L"
- board text removed: "C&K 7301MD9A"
- board text removed: "Stackup: 2116 * 1 impedance controlled 1.6mm total thickness HASL finish Blue soldermask"
